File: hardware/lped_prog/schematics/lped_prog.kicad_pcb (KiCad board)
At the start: 2 copper layers, 50 x 25 mm, 27 parts, among them J1 J-Link Header, J2 Conn_01x01_Pin, J3 Conn_01x01_Pin, J4 Conn_01x01_Pin, J5 Conn_01x01_Pin, J6 Conn_01x01_Pin, J7 USB_C_Receptacle_USB2.0_14P, J8 Power connector, J9 Conn_01x01_Pin, SW1 Connection toggle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

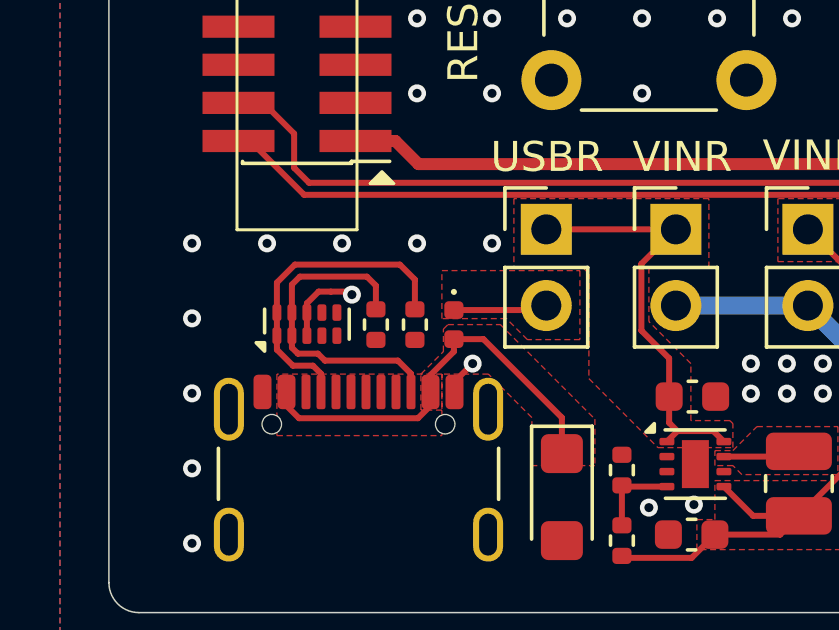
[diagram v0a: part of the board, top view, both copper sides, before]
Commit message: fix(hardware): minor fixes before manufacturing
Changed footprint of USB protection diode
Changed footprint of Programmer fuse
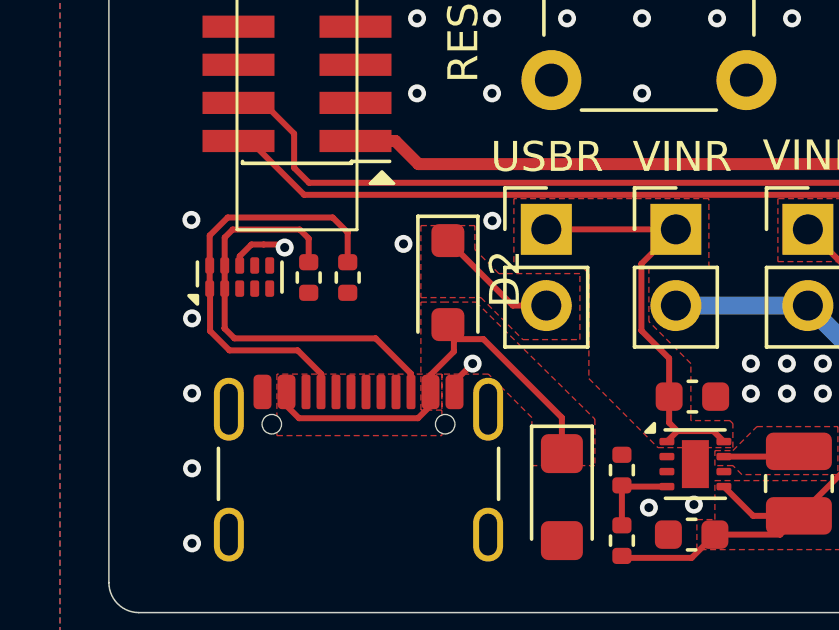
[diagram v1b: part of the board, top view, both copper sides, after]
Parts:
- D2: footprint Diode_SMD:D_0402_1005Metric -> Diode_SMD:D_SOD-123F
- moved R3 2.74 mm to (108.0, 78.8)
- moved R4 2.74 mm to (106.7, 78.8)
- moved U2 2.74 mm to (104.4, 78.8)
- moved D2 1.41 mm to (111.3, 79.0)
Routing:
- net /CC2: track 10.9 -> 14.3 mm
- net /CC1: track 10.7 -> 14.1 mm
- net Net-(D2-K): track 3.14 -> 4.39 mm
- net Earth: track 3.98 -> 3.21 mm, vias 56 -> 54
